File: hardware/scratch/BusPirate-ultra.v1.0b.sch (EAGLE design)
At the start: 166 parts, among them IC1 23LC1024, IC10 SN74LVC1T45DBV, IC11 SN74LVC1T45DBV, IC12 74LVC1G07DBV, IC13 SN74LVC1T45DBV, IC17 74LVC1G07DBV, IC18 SN74LVC1T45DBV, IC19 74LVC1G07DBV, IC2 23LC1024, IC20 SN74LVC1T45DBV, IC21 74LVC1G07DBV, IC22 SN74LVC1T45DBV, IC23 MCP1824_ADJ, IC24 74HCT4051, IC4 74LVC1G07DBV, IC5 74LVC1G07DBV, IC6 74LVC1G07DBV, IC7 74LVC1G07DBV, IC8 SN74LVC1T45DBV, IC9 SN74LVC1T45DBV, J1 CON_MOLEX_MALE_SMT_SH_1.25, J2 CON_HEADER_1X04, J4 CON_HEADER_1X10-RIGHT_ANGLED_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, Q1 DMMT3906W, U1 W25X40CL, U2 STM32F103ZX, U3 ICE40HX4K, U4 MCP6001, U5 74LVC245A, U7 MCP6001, U8 74HCT4066PW, U9 74HCT4066PW

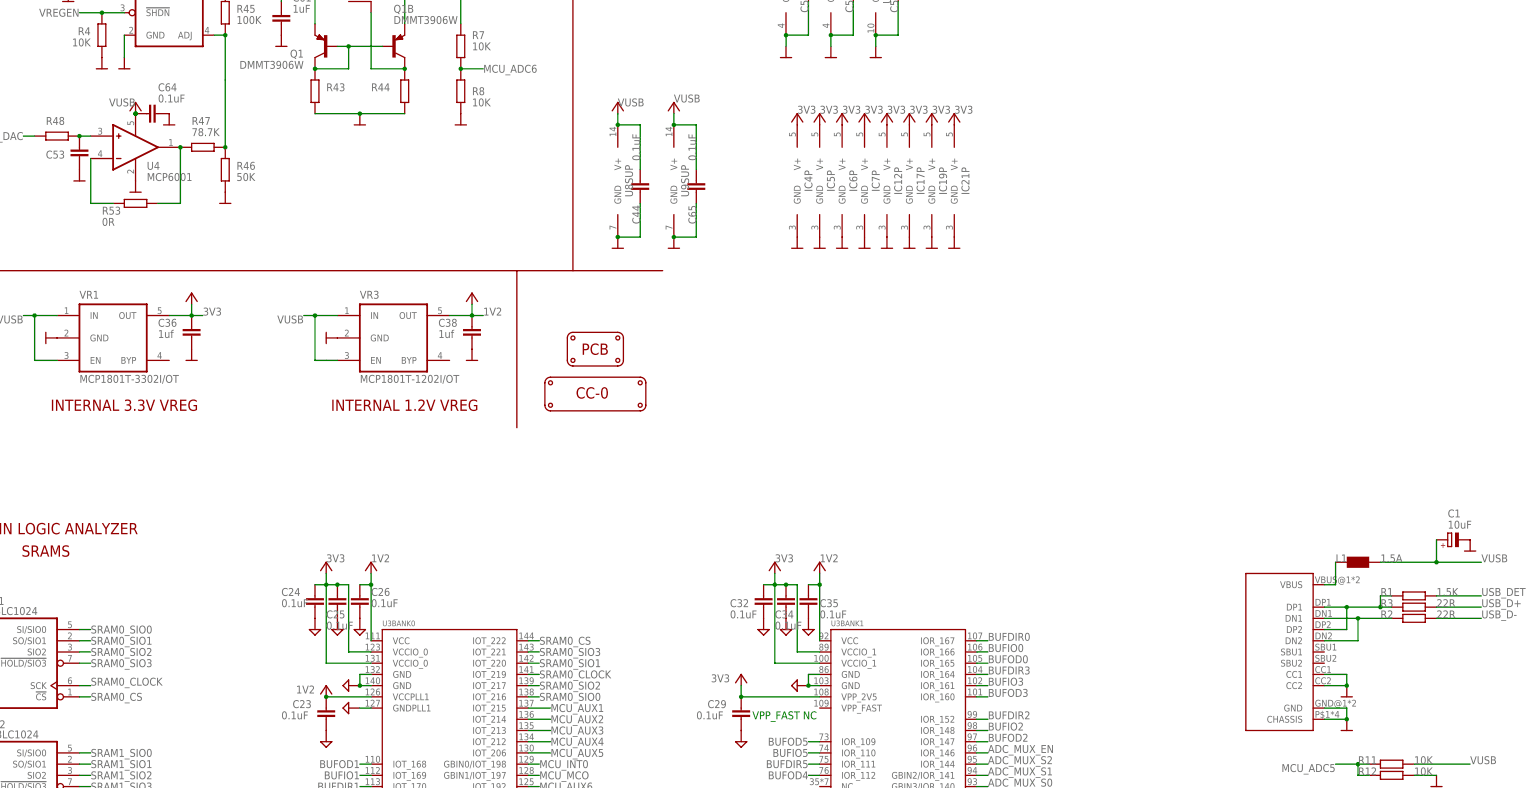
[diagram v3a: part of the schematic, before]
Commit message: move back vreg circuit down near display connector, added 5K1 resistors on each USB-C CC1 and CC2 pulling to GND
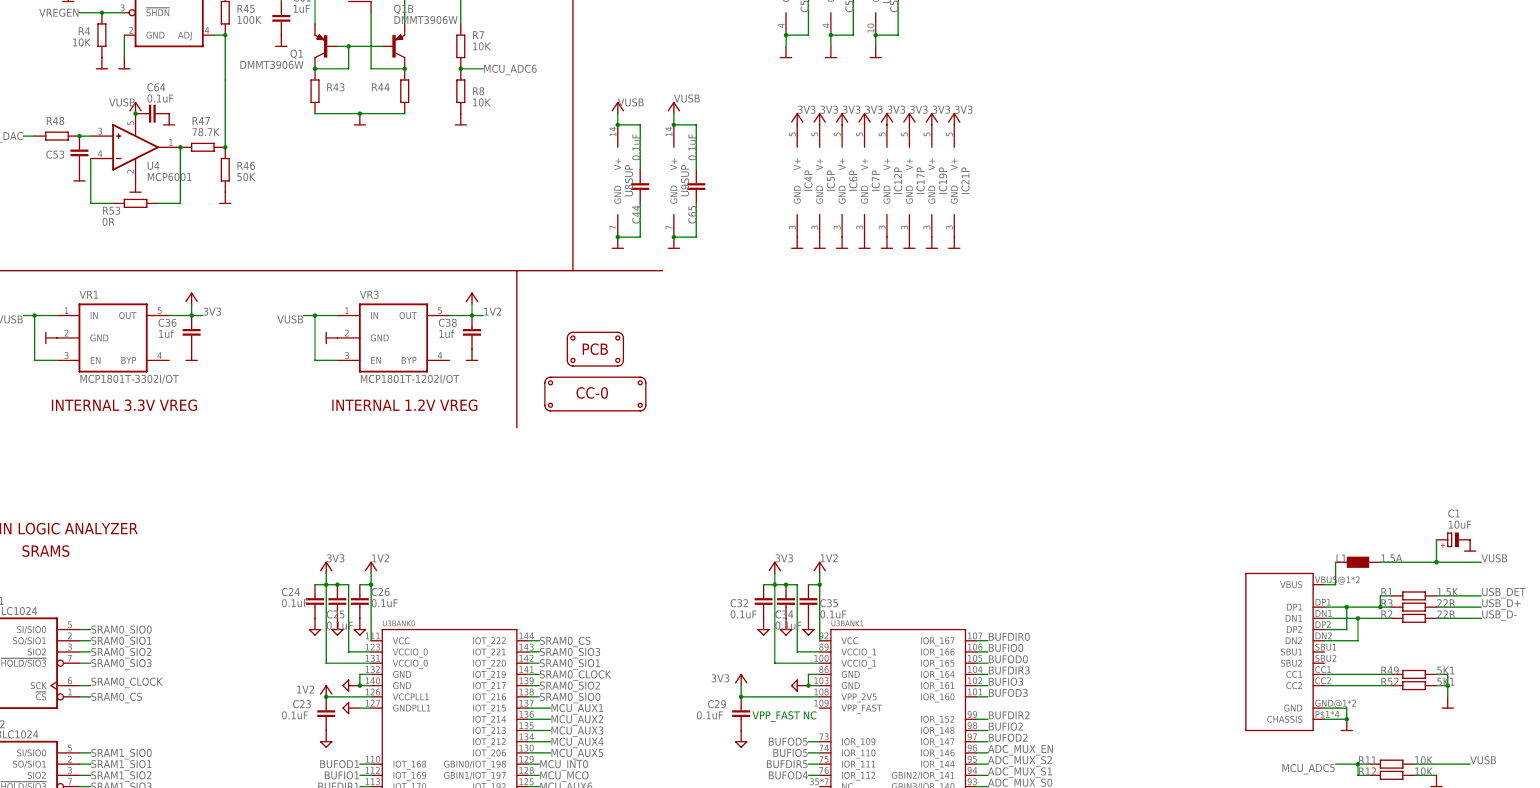
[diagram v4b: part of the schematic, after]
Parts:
- added R49, R52: 5K1, rcl:R-EU_R0603
- C53, C64: device dp_devices.v6:CAPACITOR_NPOL-0603 -> rcl:C-EUC0603
- R48: device dp_devices.v6:RESISTOR-0603 -> rcl:R-EU_R0603
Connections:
- new net N$14: R49.1, U$3.CC1
- new net N$20: R52.1, U$3.CC2
- net GND: now also R49.2, R52.2; no longer U$3.CC1, U$3.CC2
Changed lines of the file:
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@@
 <part name="C63" library="dp_devices.v6" deviceset="CAPACITOR_NPOL" device="-0603" value="10uF"/>
 <part name="GND4" library="dp_devices.v6" deviceset="SUPPLY_GND" device=""/>
-<part name="C64" library="dp_devices.v6" deviceset="CAPACITOR_NPOL" device="-0603" value="0.1uF"/>
 <part name="GND8" library="dp_devices.v6" deviceset="SUPPLY_GND" device=""/>
 <part name="Q1" library="dp_devices.v6" deviceset="TRANSISTOR-BJT_DMMT3906W" device="" value="DMMT3906W"/>
@@
 <part name="P+27" library="supply1" library_urn="urn:adsk.eagle:library:371" deviceset="VCC" device=""/>
 <part name="GND85" library="dp_devices.v6" deviceset="SUPPLY_GND" device=""/>
-<part name="C53" library="dp_devices.v6" deviceset="CAPACITOR_NPOL" device="-0603"/>
 <part name="GND22" library="dp_devices.v6" deviceset="SUPPLY_GND" device=""/>
-<part name="R48" library="dp_devices.v6" deviceset="RESISTOR" device="-0603"/>
+<part name="R48" library="rcl" library_urn="urn:adsk.eagle:library:334" deviceset="R-EU_" device="R0603" package3d_urn="urn:adsk.eagle:package:23555/3"/>
 <part name="R53" library="dp_devices.v6" deviceset="RESISTOR" device="-0603" value="0R"/>
 <part name="IC5" library="dp_devices.v6" deviceset="IC_BUFF_74LVC1G07" device="-EXTENDED" value="74LVC1G07DBV"/>
@@
 <part name="U$3" library="usbc" deviceset="USB-C-12" device=""/>
 <part name="GND13" library="dp_devices.v6" deviceset="SUPPLY_GND" device=""/>
+<part name="C53" library="rcl" library_urn="urn:adsk.eagle:library:334" deviceset="C-EU" device="C0603" package3d_urn="urn:adsk.eagle:package:23616/2"/>
+<part name="C64" library="rcl" library_urn="urn:adsk.eagle:library:334" deviceset="C-EU" device="C0603" package3d_urn="urn:adsk.eagle:package:23616/2" value="0.1uF"/>
+<part name="R49" library="rcl" library_urn="urn:adsk.eagle:library:334" deviceset="R-EU_" device="R0603" package3d_urn="urn:adsk.eagle:package:23555/3" value="5K1"/>
+<part name="R52" library="rcl" library_urn="urn:adsk.eagle:library:334" deviceset="R-EU_" device="R0603" package3d_urn="urn:adsk.eagle:package:23555/3" value="5K1"/>
 </parts>
 <sheets>
@@
 </instance>
 <instance part="GND4" gate="G$1" x="322.58" y="325.12" smashed="yes"/>
-<instance part="C64" gate="C" x="342.9" y="299.72" smashed="yes" rot="R90">
-<attribute name="NAME" x="342.9" y="304.8" size="1.778" layer="95"/>
-<attribute name="VALUE" x="342.9" y="302.26" size="1.778" layer="96"/>
-</instance>
 <instance part="GND8" gate="G$1" x="345.44" y="297.18" smashed="yes"/>
 <instance part="Q1" gate="A" x="381" y="314.96" smashed="yes" rot="MR0">
@@
 <instance part="P+27" gate="VCC" x="487.68" y="299.72" smashed="yes"/>
 <instance part="GND85" gate="G$1" x="487.68" y="269.24" smashed="yes"/>
-<instance part="C53" gate="C" x="325.12" y="289.56" smashed="yes">
-<attribute name="NAME" x="317.5" y="289.56" size="1.778" layer="95"/>
-<attribute name="VALUE" x="317.5" y="287.02" size="1.778" layer="96"/>
-</instance>
 <instance part="GND22" gate="G$1" x="325.12" y="284.48" smashed="yes"/>
-<instance part="R48" gate="R" x="320.04" y="294.64" smashed="yes">
+<instance part="R48" gate="G$1" x="320.04" y="294.64" smashed="yes">
 <attribute name="NAME" x="317.5" y="297.18" size="1.778" layer="95" font="vector"/>
 <attribute name="VALUE" x="317.5" y="297.18" size="1.778" layer="96" font="vector"/>
@@
 <instance part="GND69" gate="G$1" x="706.12" y="43.18" smashed="yes"/>
 <instance part="U$3" gate="G$1" x="581.66" y="185.42" rot="MR0"/>
-<instance part="GND13" gate="G$1" x="612.14" y="167.64" smashed="yes"/>
+<instance part="GND13" gate="G$1" x="635" y="165.1" smashed="yes"/>
+<instance part="C53" gate="G$1" x="325.12" y="292.1" smashed="yes">
+<attribute name="NAME" x="317.5" y="289.56" size="1.778" layer="95"/>
+<attribute name="VALUE" x="326.644" y="287.401" size="1.778" layer="96"/>
+</instance>
+<instance part="C64" gate="G$1" x="340.36" y="299.72" smashed="yes" rot="R90">
+<attribute name="NAME" x="340.36" y="304.8" size="1.778" layer="95"/>
+<attribute name="VALUE" x="340.36" y="302.26" size="1.778" layer="96"/>
+</instance>
+<instance part="R49" gate="G$1" x="627.38" y="172.72" smashed="yes">
+<attribute name="NAME" x="619.76" y="172.72" size="1.778" layer="95" font="vector"/>
+<attribute name="VALUE" x="632.46" y="172.72" size="1.778" layer="96" font="vector"/>
+</instance>
+<instance part="R52" gate="G$1" x="627.38" y="170.18" smashed="yes">
+<attribute name="NAME" x="619.76" y="170.18" size="1.778" layer="95" font="vector"/>
+<attribute name="VALUE" x="632.46" y="170.18" size="1.778" layer="96" font="vector"/>
+</instance>
 </instances>
 <busses>
@@
 </segment>
 <segment>
-<pinref part="C64" gate="C" pin="2"/>
-<pinref part="GND8" gate="G$1" pin="GND"/>
-</segment>
-<segment>
 <pinref part="IC23" gate="IC" pin="GND"/>
 <pinref part="GND9" gate="G$1" pin="GND"/>
@@
 </segment>
 <segment>
-<pinref part="GND22" gate="G$1" pin="GND"/>
-<pinref part="C53" gate="C" pin="2"/>
-</segment>
-<segment>
 <pinref part="IC5" gate="P" pin="GND"/>
 <pinref part="GND25" gate="G$1" pin="GND"/>
@@
 </segment>
 <segment>
-<pinref part="U$3" gate="G$1" pin="CC1"/>
+<pinref part="GND22" gate="G$1" pin="GND"/>
+<pinref part="C53" gate="G$1" pin="2"/>
+</segment>
+<segment>
+<pinref part="GND8" gate="G$1" pin="GND"/>
+<pinref part="C64" gate="G$1" pin="2"/>
+</segment>
+<segment>
+<pinref part="R49" gate="G$1" pin="2"/>
+<wire x1="632.46" y1="172.72" x2="635" y2="172.72" width="0.1524" layer="91"/>
 <pinref part="GND13" gate="G$1" pin="GND"/>
-<wire x1="607.06" y1="172.72" x2="612.14" y2="172.72" width="0.1524" layer="91"/>
-<wire x1="612.14" y1="172.72" x2="612.14" y2="170.18" width="0.1524" layer="91"/>
-<pinref part="U$3" gate="G$1" pin="CC2"/>
-<wire x1="607.06" y1="170.18" x2="612.14" y2="170.18" width="0.1524" layer="91"/>
-<junction x="612.14" y="170.18"/>
+<wire x1="635" y1="172.72" x2="635" y2="170.18" width="0.1524" layer="91"/>
+<pinref part="R52" gate="G$1" pin="2"/>
+<wire x1="635" y1="170.18" x2="635" y2="167.64" width="0.1524" layer="91"/>
+<wire x1="632.46" y1="170.18" x2="635" y2="170.18" width="0.1524" layer="91"/>
+<junction x="635" y="170.18"/>
 </segment>
 </net>
@@
 <segment>
 <pinref part="U4" gate="U" pin="V+"/>
-<pinref part="C64" gate="C" pin="1"/>
 <pinref part="SUPPLY5" gate="1" pin="V+"/>
-<junction x="337.82" y="299.72"/>
-<junction x="337.82" y="299.72"/>
 <label x="337.82" y="302.26" size="1.778" layer="95" align="center-right"/>
+<pinref part="C64" gate="G$1" pin="1"/>
+<junction x="337.82" y="299.72"/>
+<pinref part="C64" gate="G$1" pin="1"/>
 </segment>
 <segment>
@@
 </segment>
 <segment>
-<pinref part="R48" gate="R" pin="1"/>
+<pinref part="R48" gate="G$1" pin="1"/>
 <wire x1="314.96" y1="294.64" x2="312.42" y2="294.64" width="0.1524" layer="91"/>
 <label x="312.42" y="294.64" size="1.778" layer="95" align="center-right"/>
@@
 <net name="N$31" class="0">
 <segment>
-<pinref part="C53" gate="C" pin="1"/>
-<pinref part="R48" gate="R" pin="2"/>
+<pinref part="R48" gate="G$1" pin="2"/>
 <pinref part="U4" gate="U" pin="+"/>
 <wire x1="327.66" y1="294.64" x2="325.12" y2="294.64" width="0.1524" layer="91"/>
+<pinref part="C53" gate="G$1" pin="1"/>
 <junction x="325.12" y="294.64"/>
 </segment>
@@
 </segment>
 </net>
+<net name="N$14" class="0">
+<segment>
+<pinref part="R49" gate="G$1" pin="1"/>
+<pinref part="U$3" gate="G$1" pin="CC1"/>
+<wire x1="622.3" y1="172.72" x2="607.06" y2="172.72" width="0.1524" layer="91"/>
+</segment>
+</net>
+<net name="N$20" class="0">
+<segment>
+<pinref part="R52" gate="G$1" pin="1"/>
+<pinref part="U$3" gate="G$1" pin="CC2"/>
+<wire x1="622.3" y1="170.18" x2="607.06" y2="170.18" width="0.1524" layer="91"/>
+</segment>
+</net>
